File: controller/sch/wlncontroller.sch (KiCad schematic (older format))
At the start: 4 parts

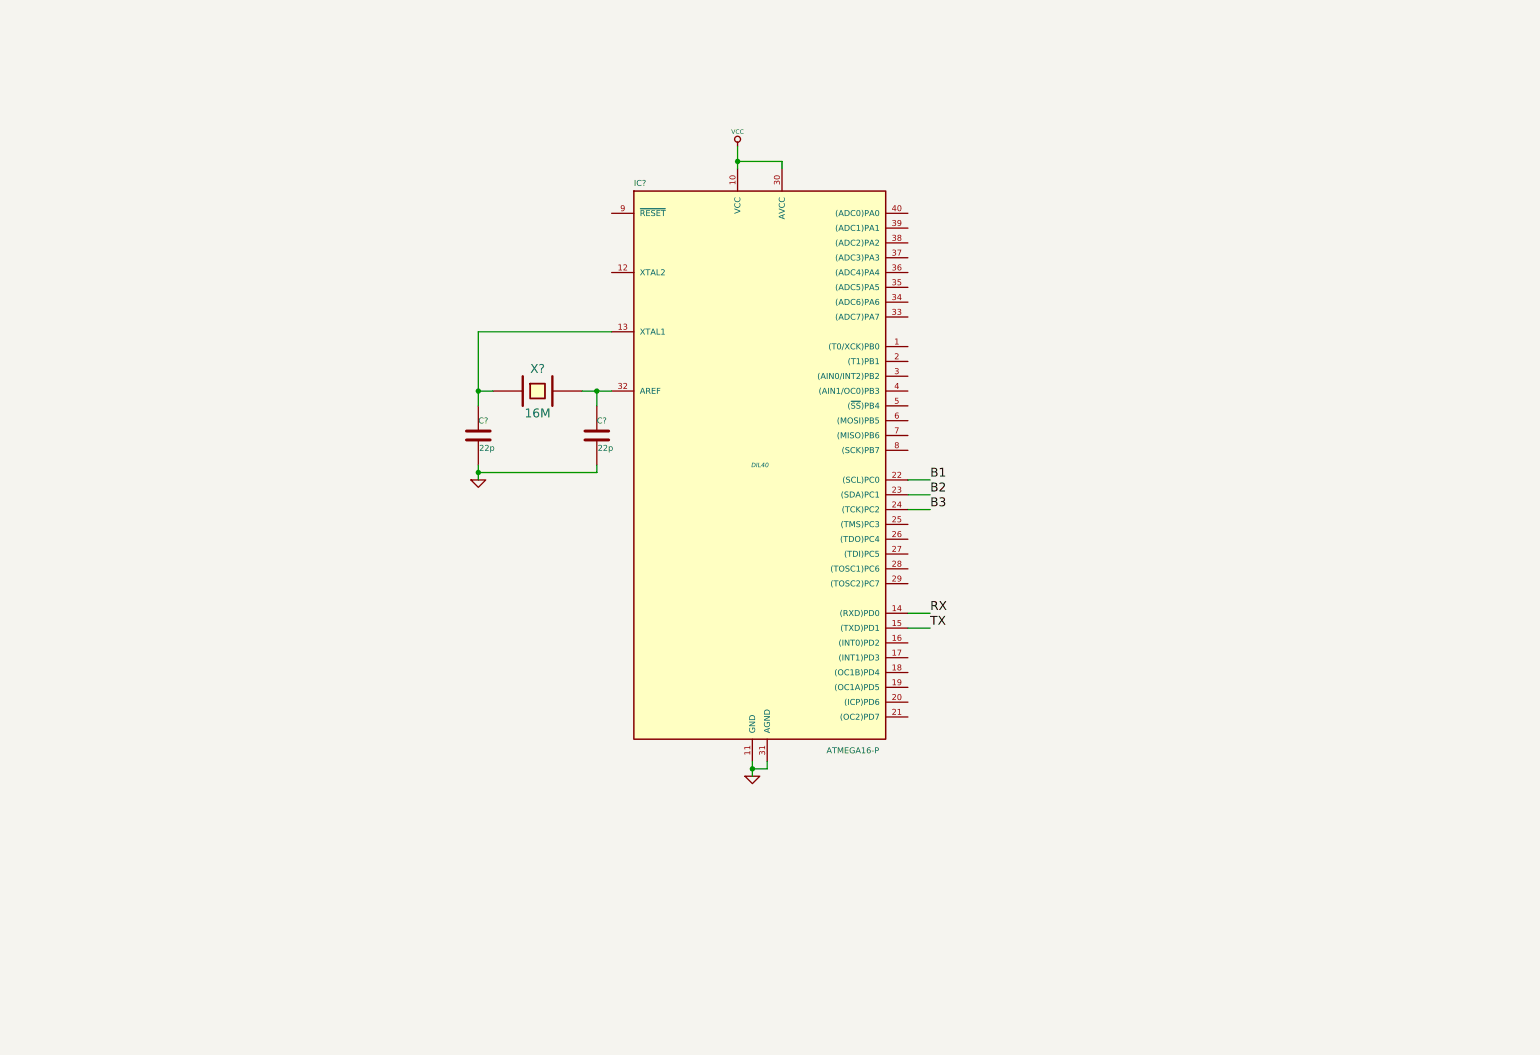
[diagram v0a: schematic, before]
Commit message: controller implementation of all buttons, clean-up
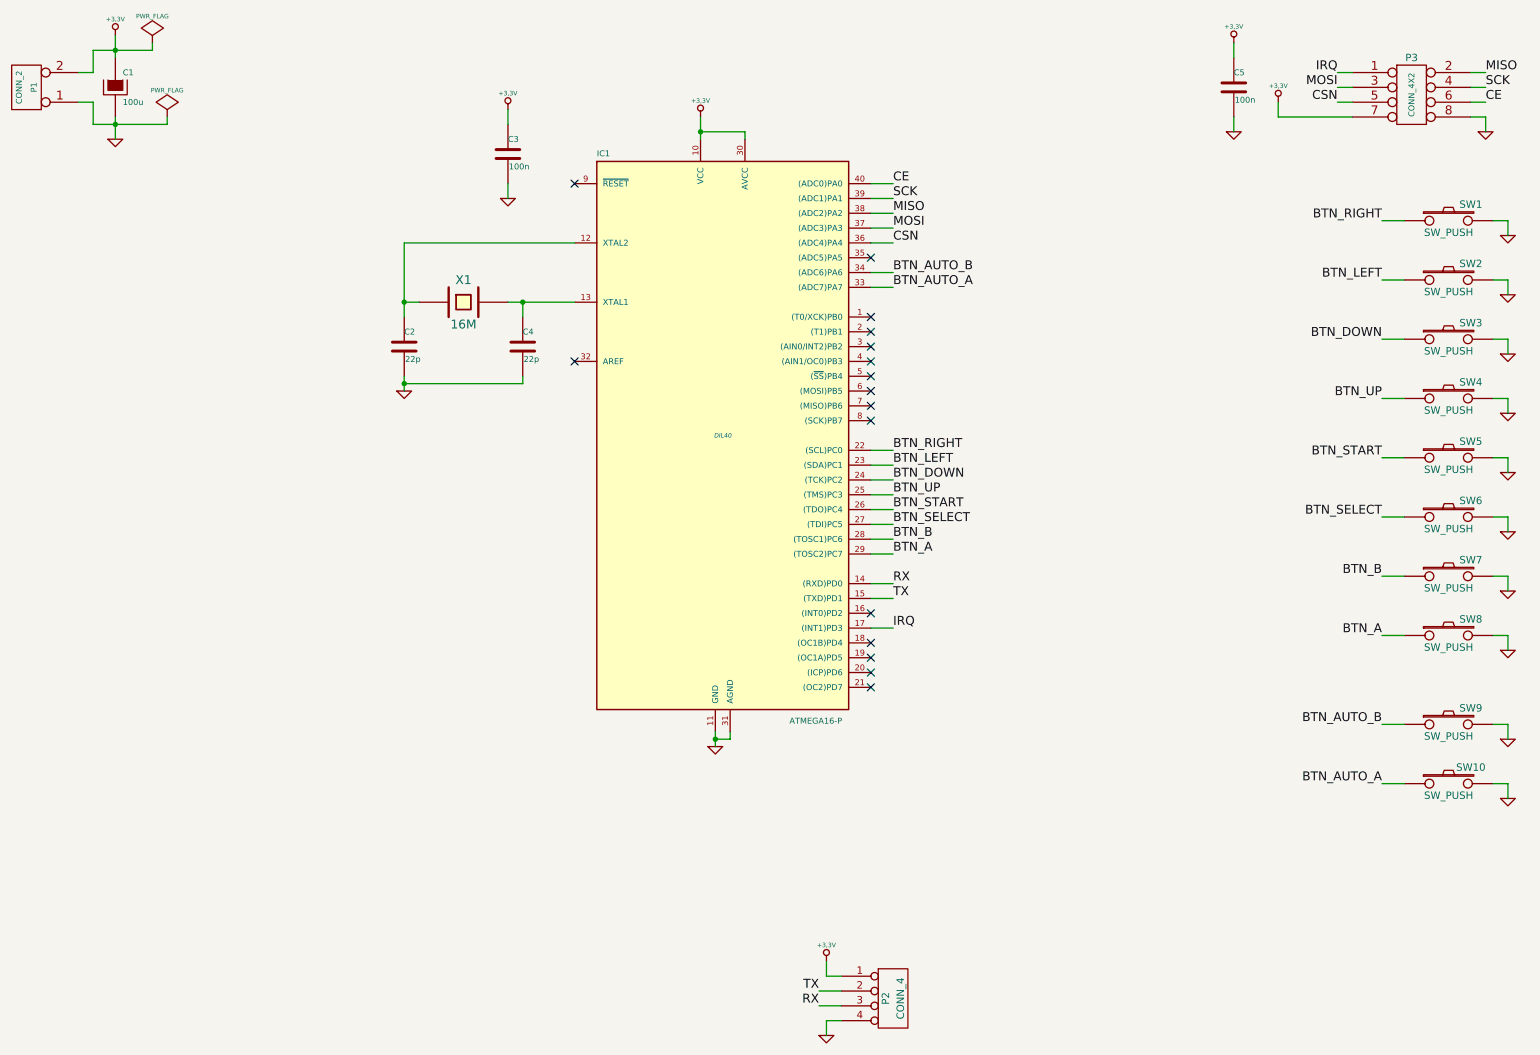
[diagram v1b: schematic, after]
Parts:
- added C1: 100u, symbol CAPAPOL
- added C3, C5: 100n, symbol C
- added P1: CONN_2, symbol CONN_2
- added P2: CONN_4, symbol CONN_4
- added P3: CONN_4X2, symbol CONN_4X2
- added SW1, SW10, SW2, SW3, SW4, SW5, SW6, SW7, SW8, SW9: SW_PUSH, symbol SW_PUSH
- gave numbers to parts that had none: 4
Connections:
- net GND: now also C1.2, C3.2, C5.2, P1.1 (P1), P2.4 (P4), P3.8, SW1.2, SW10.2, SW2.2, SW3.2, SW4.2, SW5.2, SW6.2, SW7.2, SW8.2, SW9.2
- net RX: now also P2.3 (P3)
- net TX: now also P2.2 (P2)
- net at IC1.12 (XTAL2): now also C2.1, X1.1
- net IRQ: now reaches IC1.17 ((INT1)PD3)
- net IRQ: now also P3.1
- net BTN_UP: now reaches IC1.25 ((TMS)PC3)
- net BTN_UP: now also SW4.1
- net BTN_START: now reaches IC1.26 ((TDO)PC4)
- net BTN_START: now also SW5.1
- net BTN_SELECT: now reaches IC1.27 ((TDI)PC5)
- net BTN_SELECT: now also SW6.1
- net BTN_B: now reaches IC1.28 ((TOSC1)PC6)
- net BTN_B: now also SW7.1
- net BTN_A: now reaches IC1.29 ((TOSC2)PC7)
- net BTN_A: now also SW8.1
- net at C4.1, X1.2: now also IC1.13 (XTAL1); no longer IC1.32 (AREF)
- net BTN_AUTO_A: now reaches IC1.33 ((ADC7)PA7)
- net BTN_AUTO_A: now also SW10.1
- net BTN_AUTO_B: now reaches IC1.34 ((ADC6)PA6)
- net BTN_AUTO_B: now also SW9.1
- net CSN: now reaches IC1.36 ((ADC4)PA4)
- net CSN: now also P3.5
- net MOSI: now reaches IC1.37 ((ADC3)PA3)
- net MOSI: now also P3.3
- net MISO: now reaches IC1.38 ((ADC2)PA2)
- net MISO: now also P3.2
- net SCK: now reaches IC1.39 ((ADC1)PA1)
- net SCK: now also P3.4
- net CE: now reaches IC1.40 ((ADC0)PA0)
- net CE: now also P3.6
- net B1 renamed BTN_RIGHT
- net BTN_RIGHT: now also SW1.1
- net B2 renamed BTN_LEFT
- net BTN_LEFT: now also SW2.1
- net B3 renamed BTN_DOWN
- net BTN_DOWN: now also SW3.1
- net VCC renamed +3.3V
- net +3.3V: now also C1.1, C3.1, C5.1, P1.2 (PM), P2.1 (P1), P3.7
- no-connect marks 0 -> 16
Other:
- moved on the sheet: C2, C4, IC1, X1
